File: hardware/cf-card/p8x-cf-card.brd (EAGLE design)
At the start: 160 x 100 mm, 17 parts, among them J1 DIN41612-96M, J2 CF/IDE 40P, U1 DATA BUF, U2 IO PAGE, U3 DOE DEC, U4 DLD DEC, U5 74HCT14, U6 74HCT10, U7 74HCT10, U8 74HCT08

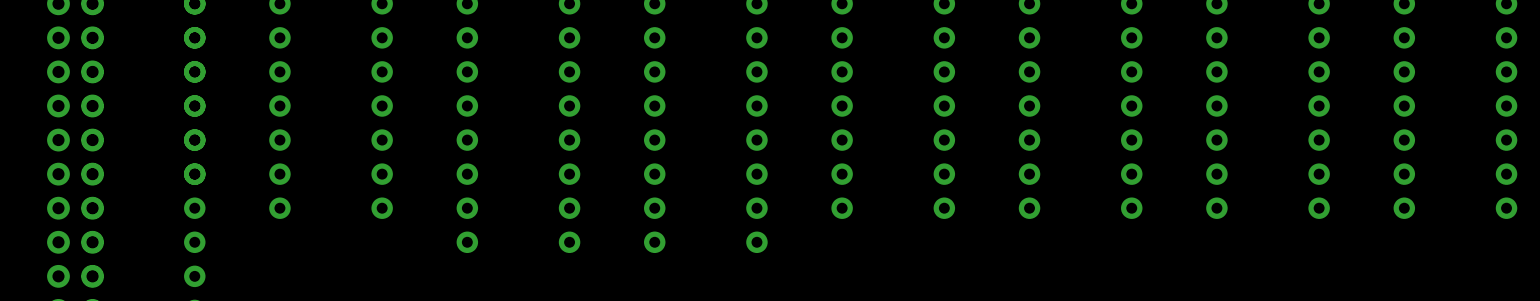
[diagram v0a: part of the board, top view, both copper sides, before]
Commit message: hw: per-IC 100nF decoupling caps on every card
card standards sec.5 requires a decoupling cap per IC; only the backplane had
them. gen_eagle's card() now generates one 100nF cap (CDn, C_DISC footprint)
per IC on the five plug-in cards, placed next to its IC and wired VCC<->GND;
the memory card's separate build does the same for U1-U9.

Caps added: control 18, regbank 44, alu 31, io 15, cf 8, memory 9. All 7
boards regenerate with 0 validation errors; card schematic PDFs refreshed.
Placement is approximate (caps sit just below each IC) pending Fusion routing.

Clears a pre-fab blocker from the backlog.

Co-Authored-By: Claude Opus 4.8 <noreply@anthropic.com>
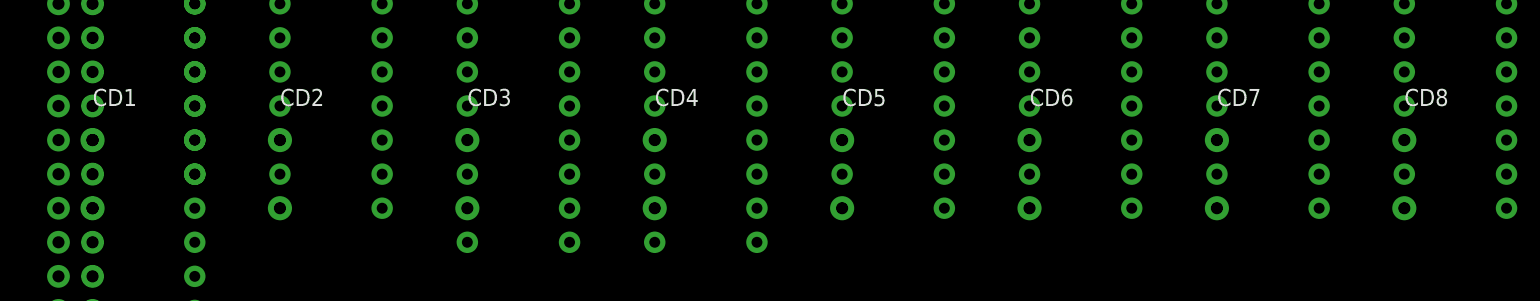
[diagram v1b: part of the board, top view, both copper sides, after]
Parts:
- added CD1, CD2, CD3, CD4, CD5, CD6, CD7, CD8: 100N, p8x:C_DISC
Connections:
- net GND: now also CD1.2, CD2.2, CD3.2, CD4.2, CD5.2, CD6.2, CD7.2, CD8.2
- net VCC: now also CD1.1, CD2.1, CD3.1, CD4.1, CD5.1, CD6.1, CD7.1, CD8.1
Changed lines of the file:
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@@
 <element name="J1" library="p8x" package="DIN96" value="DIN41612-96M" x="147.32" y="88.90"/>
 <element name="U1" library="p8x" package="DIP20" value="DATA BUF" x="7.62" y="88.90"/>
+<element name="CD1" library="p8x" package="C_DISC" value="100N" x="7.62" y="78.74"/>
 <element name="U2" library="p8x" package="DIP14" value="IO PAGE" x="21.59" y="88.90"/>
+<element name="CD2" library="p8x" package="C_DISC" value="100N" x="21.59" y="78.74"/>
 <element name="U3" library="p8x" package="DIP16" value="DOE DEC" x="35.56" y="88.90"/>
+<element name="CD3" library="p8x" package="C_DISC" value="100N" x="35.56" y="78.74"/>
 <element name="U4" library="p8x" package="DIP16" value="DLD DEC" x="49.53" y="88.90"/>
+<element name="CD4" library="p8x" package="C_DISC" value="100N" x="49.53" y="78.74"/>
 <element name="U5" library="p8x" package="DIP14" value="74HCT14" x="63.50" y="88.90"/>
+<element name="CD5" library="p8x" package="C_DISC" value="100N" x="63.50" y="78.74"/>
 <element name="U6" library="p8x" package="DIP14" value="74HCT10" x="77.47" y="88.90"/>
+<element name="CD6" library="p8x" package="C_DISC" value="100N" x="77.47" y="78.74"/>
 <element name="U7" library="p8x" package="DIP14" value="74HCT10" x="91.44" y="88.90"/>
+<element name="CD7" library="p8x" package="C_DISC" value="100N" x="91.44" y="78.74"/>
 <element name="U8" library="p8x" package="DIP14" value="74HCT08" x="105.41" y="88.90"/>
+<element name="CD8" library="p8x" package="C_DISC" value="100N" x="105.41" y="78.74"/>
 <element name="J2" library="p8x" package="HDR40" value="CF/IDE 40P" x="5.08" y="96.52"/>
 <element name="RN1" library="p8x" package="SIP9" value="8X10K" x="15.24" y="96.52"/>
@@
 <contactref element="J1" pad="C31"/>
 <contactref element="J1" pad="C32"/>
+<contactref element="CD1" pad="2"/>
+<contactref element="CD2" pad="2"/>
+<contactref element="CD3" pad="2"/>
+<contactref element="CD4" pad="2"/>
+<contactref element="CD5" pad="2"/>
+<contactref element="CD6" pad="2"/>
+<contactref element="CD7" pad="2"/>
+<contactref element="CD8" pad="2"/>
 <polygon width="0.254" layer="2" isolate="0.3" rank="1">
 <vertex x="0" y="0"/>
@@
 <contactref element="J1" pad="C1"/>
 <contactref element="J1" pad="C2"/>
+<contactref element="CD1" pad="1"/>
+<contactref element="CD2" pad="1"/>
+<contactref element="CD3" pad="1"/>
+<contactref element="CD4" pad="1"/>
+<contactref element="CD5" pad="1"/>
+<contactref element="CD6" pad="1"/>
+<contactref element="CD7" pad="1"/>
+<contactref element="CD8" pad="1"/>
 <polygon width="0.254" layer="15" isolate="0.3" rank="1">
 <vertex x="0" y="0"/>

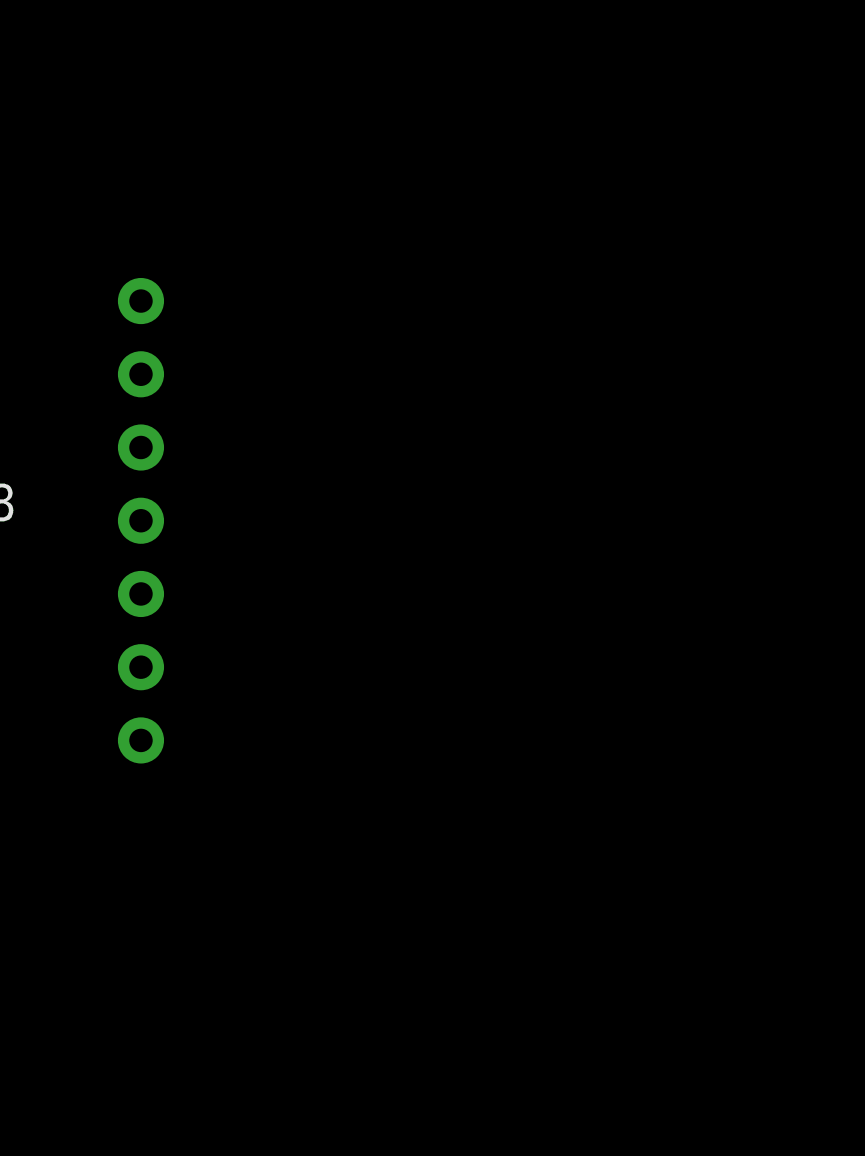
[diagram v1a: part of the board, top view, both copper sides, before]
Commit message: feat(hw): provision RTC + CF 8-bit fallback footprints (rev C, DNP)
The last two pre-fab board items, both Do-Not-Populate so the options exist
post-fab without a respin.

- I/O card: DS1302 RTC (U16) + 32.768kHz crystal (X3) + backup coin cell (BT1)
  + a 3-wire breakout header (J3). Fully isolated peripheral (crystal across
  X1/X2, VCC1 from +5, VCC2 from the cell, CE/SCLK/IO to J3) — no bus contention
  possible. Reserved I/O address $FF08 (PORT DEC U2 Y3). Crystal + coin-cell use
  placeholder THT footprints; VERIFY land patterns against real parts before fab.
- CF card: 8-bit fallback latch (U9, 74374). CF high data byte D8-15 wired to its
  inputs; output forced high-Z and clock grounded (inert). Populate + wire the
  bus output + decode only if a CF card refuses 8-bit mode (drives the data bus,
  so design with DRC).
- New device defs DS1302/XTAL32/COIN + a DIP8 package.

All 7 boards regenerate with 0 validation errors; all 6 test suites pass.

Co-Authored-By: Claude Opus 4.8 <noreply@anthropic.com>
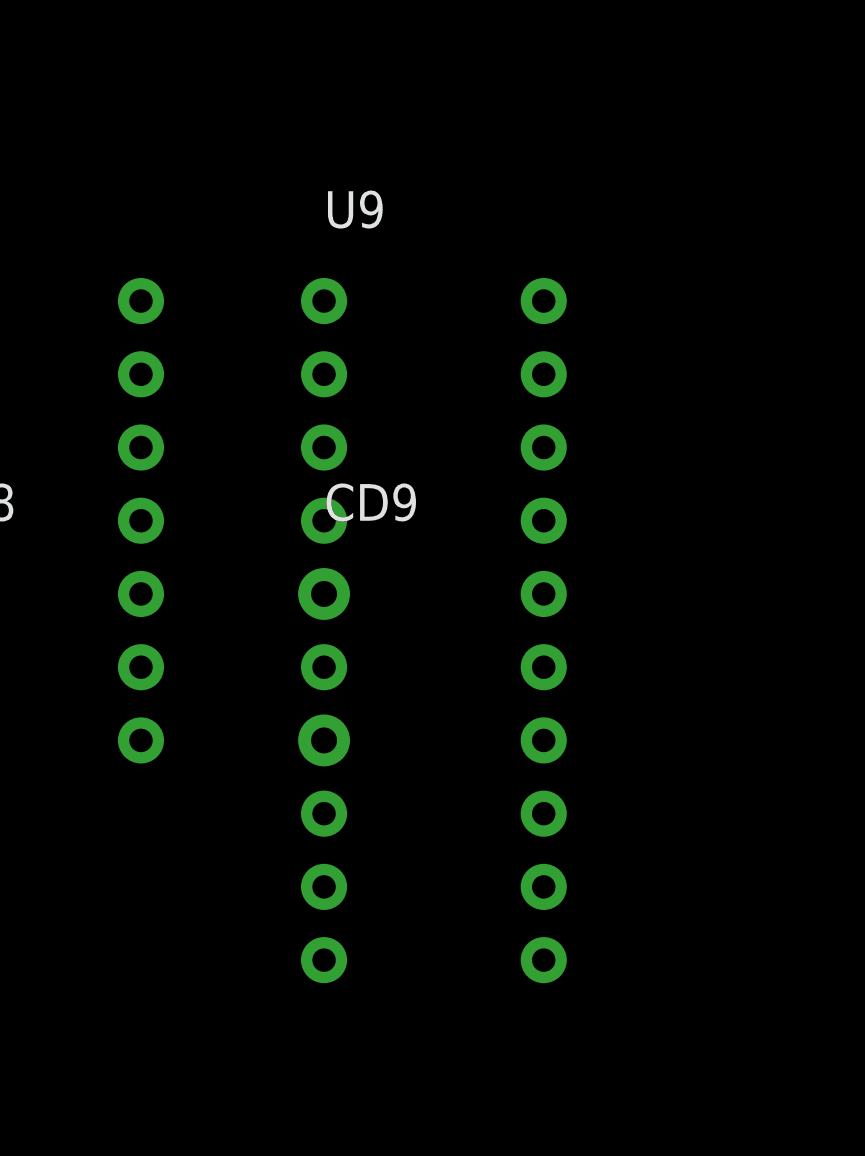
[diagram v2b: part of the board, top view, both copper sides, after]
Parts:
- added CD9: 100N, p8x:C_DISC
- added U9: CF HI-BYTE DNP, p8x:DIP20
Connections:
- new net CFD10: J2.8, U9.7
- new net CFD11: J2.10, U9.8
- new net CFD12: J2.12, U9.13
- new net CFD13: J2.14, U9.14
- new net CFD14: J2.16, U9.17
- new net CFD15: J2.18, U9.18
- new net CFD8: J2.4, U9.3
- new net CFD9: J2.6, U9.4
- net GND: now also CD9.2, U9.11
- net VCC: now also CD9.1, U9.1
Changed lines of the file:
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@@
 <element name="U8" library="p8x" package="DIP14" value="74HCT08" x="105.41" y="88.90"/>
 <element name="CD8" library="p8x" package="C_DISC" value="100N" x="105.41" y="78.74"/>
+<element name="U9" library="p8x" package="DIP20" value="CF HI-BYTE DNP" x="119.38" y="88.90"/>
+<element name="CD9" library="p8x" package="C_DISC" value="100N" x="119.38" y="78.74"/>
 <element name="J2" library="p8x" package="HDR40" value="CF/IDE 40P" x="5.08" y="96.52"/>
 <element name="RN1" library="p8x" package="SIP9" value="8X10K" x="15.24" y="96.52"/>
@@
 <contactref element="J2" pad="15"/>
 </signal>
+<signal name="CFD10">
+<contactref element="U9" pad="7"/>
+<contactref element="J2" pad="8"/>
+</signal>
+<signal name="CFD11">
+<contactref element="U9" pad="8"/>
+<contactref element="J2" pad="10"/>
+</signal>
+<signal name="CFD12">
+<contactref element="U9" pad="13"/>
+<contactref element="J2" pad="12"/>
+</signal>
+<signal name="CFD13">
+<contactref element="U9" pad="14"/>
+<contactref element="J2" pad="14"/>
+</signal>
+<signal name="CFD14">
+<contactref element="U9" pad="17"/>
+<contactref element="J2" pad="16"/>
+</signal>
+<signal name="CFD15">
+<contactref element="U9" pad="18"/>
+<contactref element="J2" pad="18"/>
+</signal>
 <signal name="CFD2">
 <contactref element="U1" pad="16"/>
@@
 <contactref element="U1" pad="11"/>
 <contactref element="J2" pad="3"/>
+</signal>
+<signal name="CFD8">
+<contactref element="U9" pad="3"/>
+<contactref element="J2" pad="4"/>
+</signal>
+<signal name="CFD9">
+<contactref element="U9" pad="4"/>
+<contactref element="J2" pad="6"/>
 </signal>
 <signal name="CLKB">
@@
 <contactref element="U7" pad="11"/>
 <contactref element="U5" pad="13"/>
+<contactref element="U9" pad="11"/>
 <contactref element="J1" pad="A31"/>
 <contactref element="J1" pad="A32"/>
@@
 <contactref element="CD7" pad="2"/>
 <contactref element="CD8" pad="2"/>
+<contactref element="CD9" pad="2"/>
 <polygon width="0.254" layer="2" isolate="0.3" rank="1">
 <vertex x="0" y="0"/>
@@
 <contactref element="R4" pad="1"/>
 <contactref element="R5" pad="1"/>
+<contactref element="U9" pad="1"/>
 <contactref element="J1" pad="A1"/>
 <contactref element="J1" pad="A2"/>
@@
 <contactref element="CD7" pad="1"/>
 <contactref element="CD8" pad="1"/>
+<contactref element="CD9" pad="1"/>
 <polygon width="0.254" layer="15" isolate="0.3" rank="1">
 <vertex x="0" y="0"/>
